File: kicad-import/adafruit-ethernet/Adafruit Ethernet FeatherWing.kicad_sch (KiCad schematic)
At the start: 48 parts

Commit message: Add initial annotation.
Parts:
- gave numbers to parts that had none: 48

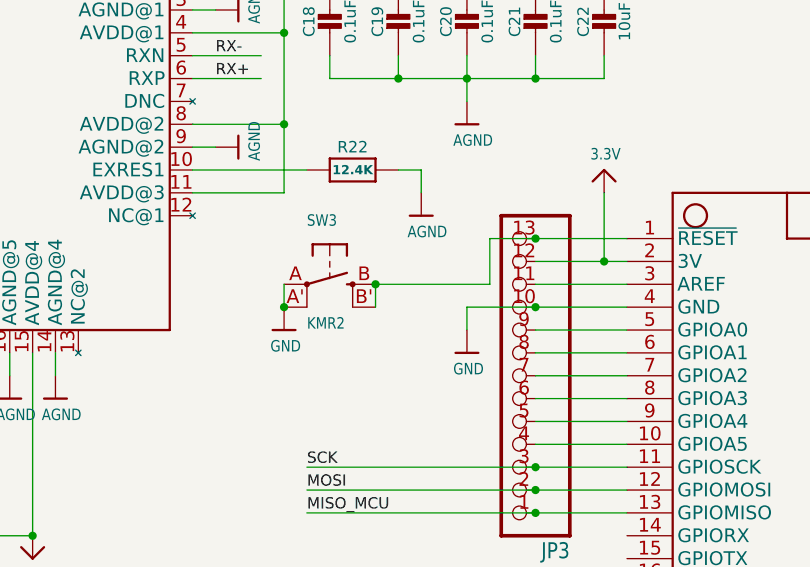
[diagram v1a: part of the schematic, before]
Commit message: Remove extra reset switches. Update notes.
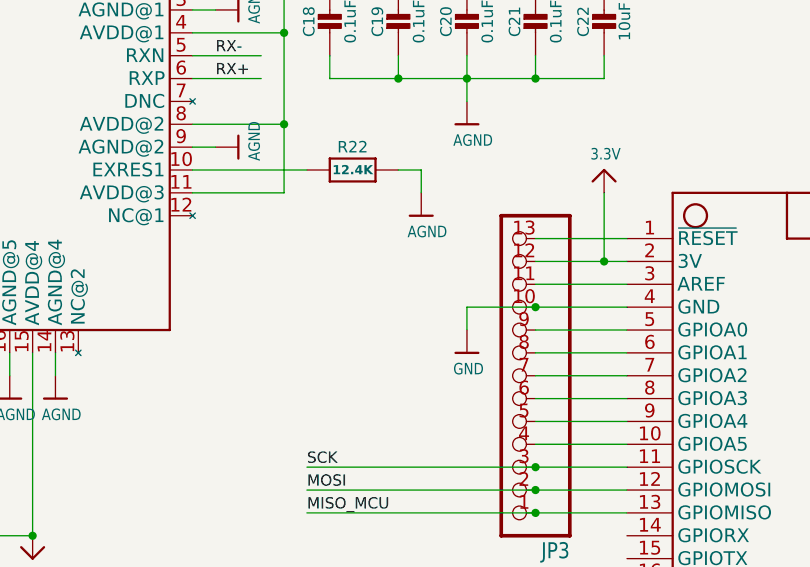
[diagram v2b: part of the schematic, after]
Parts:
- removed SW3: KMR2, Adafruit Ethernet FeatherWing:BTN_KMR2_4.6X2.8, symbol Adafruit Ethernet FeatherWing-eagle-import:SWITCH_TACT_SMT4.6X2.8
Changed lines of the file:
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@@
 	)
 	(junction
-		(at 154.94 106.68)
-		(diameter 0)
-		(color 0 0 0 0)
-	)
-	(junction
 		(at 154.94 88.9)
 		(diameter 0)
@@
 	)
 	(junction
-		(at 127 114.3)
-		(diameter 0)
-		(color 0 0 0 0)
-	)
-	(junction
 		(at 139.7 76.2)
 		(diameter 0)
@@
 	)
 	(junction
-		(at 137.16 111.76)
-		(diameter 0)
-		(color 0 0 0 0)
-	)
-	(junction
 		(at 213.36 132.08)
 		(diameter 0)
@@
 	(wire
 		(pts
-			(xy 137.16 111.76) (xy 137.16 114.3)
-		)
-		(stroke
-			(width 0.1524)
-			(type solid)
-		)
-	)
-	(wire
-		(pts
 			(xy 213.36 121.92) (xy 208.28 121.92)
 		)
@@
 	(wire
 		(pts
-			(xy 149.86 111.76) (xy 149.86 106.68)
-		)
-		(stroke
-			(width 0.1524)
-			(type solid)
-		)
-	)
-	(wire
-		(pts
 			(xy 40.64 99.06) (xy 40.64 101.6)
 		)
@@
 	(wire
 		(pts
-			(xy 127 111.76) (xy 127 114.3)
-		)
-		(stroke
-			(width 0.1524)
-			(type solid)
-		)
-	)
-	(wire
-		(pts
 			(xy 154.94 86.36) (xy 154.94 88.9)
 		)
@@
 	(wire
 		(pts
-			(xy 137.16 111.76) (xy 149.86 111.76)
-		)
-		(stroke
-			(width 0.1524)
-			(type solid)
-		)
-	)
-	(wire
-		(pts
 			(xy 76.2 58.42) (xy 76.2 55.88)
 		)
@@
 	(wire
 		(pts
-			(xy 149.86 106.68) (xy 154.94 106.68)
-		)
-		(stroke
-			(width 0.1524)
-			(type solid)
-		)
-	)
-	(wire
-		(pts
 			(xy 165.1 109.22) (xy 162.56 109.22)
 		)
@@
 	)
 	(symbol
-		(lib_id "Adafruit Ethernet FeatherWing-eagle-import:GND")
-		(at 127 116.84 0)
-		(unit 1)
-		(exclude_from_sim no)
-		(in_bom yes)
-		(on_board yes)
-		(dnp no)
-		(property "Reference" "#U$069"
-			(at 127 116.84 0)
-			(effects
-				(font
-					(size 1.27 1.27)
-				)
-				(hide yes)
-			)
-		)
-		(property "Value" "GND"
-			(at 125.476 119.38 0)
-			(effects
-				(font
-					(size 1.27 1.0795)
-				)
-				(justify left bottom)
-			)
-		)
-		(property "Footprint" ""
-			(at 127 116.84 0)
-			(effects
-				(font
-					(size 1.27 1.27)
-				)
-				(hide yes)
-			)
-		)
-		(property "Datasheet" ""
-			(at 127 116.84 0)
-			(effects
-				(font
-					(size 1.27 1.27)
-				)
-				(hide yes)
-			)
-		)
-		(property "Description" ""
-			(at 127 116.84 0)
-			(effects
-				(font
-					(size 1.27 1.27)
-				)
-				(hide yes)
-			)
-		)
-		(pin "1"
-		)
-		(instances
-			(project "Genesis"
-				(path "/66b8af00-4ede-44e3-a762-88857219665d/34668455-eab9-44a0-a7b2-48f3dfe2249d"
-					(reference "#U$069")
-					(unit 1)
-				)
-			)
-			(project ""
-				(path "/f8d80f0f-4921-491b-a5b2-8dada69d1b2b"
-					(reference "#U$47")
-					(unit 1)
-				)
-			)
-		)
-	)
-	(symbol
 		(lib_id "Adafruit Ethernet FeatherWing-eagle-import:AGND")
 		(at 88.9 154.94 0)
@@
 					(unit 1)
 				)
-			)
-		)
-	)
-	(symbol
-		(lib_id "Adafruit Ethernet FeatherWing-eagle-import:SWITCH_TACT_SMT4.6X2.8")
-		(at 132.08 111.76 0)
-		(unit 1)
-		(exclude_from_sim no)
-		(in_bom yes)
-		(on_board yes)
-		(dnp no)
-		(property "Reference" "SW3"
-			(at 129.54 105.41 0)
-			(effects
-				(font
-					(size 1.27 1.0795)
-				)
-				(justify left bottom)
-			)
-		)
-		(property "Value" "KMR2"
-			(at 129.54 116.84 0)
-			(effects
-				(font
-					(size 1.27 1.0795)
-				)
-				(justify left bottom)
-			)
-		)
-		(property "Footprint" "Adafruit Ethernet FeatherWing:BTN_KMR2_4.6X2.8"
-			(at 132.08 111.76 0)
-			(effects
-				(font
-					(size 1.27 1.27)
-				)
-				(hide yes)
-			)
-		)
-		(property "Datasheet" ""
-			(at 132.08 111.76 0)
-			(effects
-				(font
-					(size 1.27 1.27)
-				)
-				(hide yes)
-			)
-		)
-		(property "Description" ""
-			(at 132.08 111.76 0)
-			(effects
-				(font
-					(size 1.27 1.27)
-				)
-				(hide yes)
-			)
-		)
-		(pin "A"
-		)
-		(pin "A'"
-		)
-		(pin "B"
-		)
-		(pin "B'"
-		)
-		(instances
-			(project "Genesis"
-				(path "/66b8af00-4ede-44e3-a762-88857219665d/34668455-eab9-44a0-a7b2-48f3dfe2249d"
-					(reference "SW3")
-					(unit 1)
-				)
-			)
-			(project ""
-				(path "/f8d80f0f-4921-491b-a5b2-8dada69d1b2b"
-					(reference "SW1")
-					(unit 1)
-				)

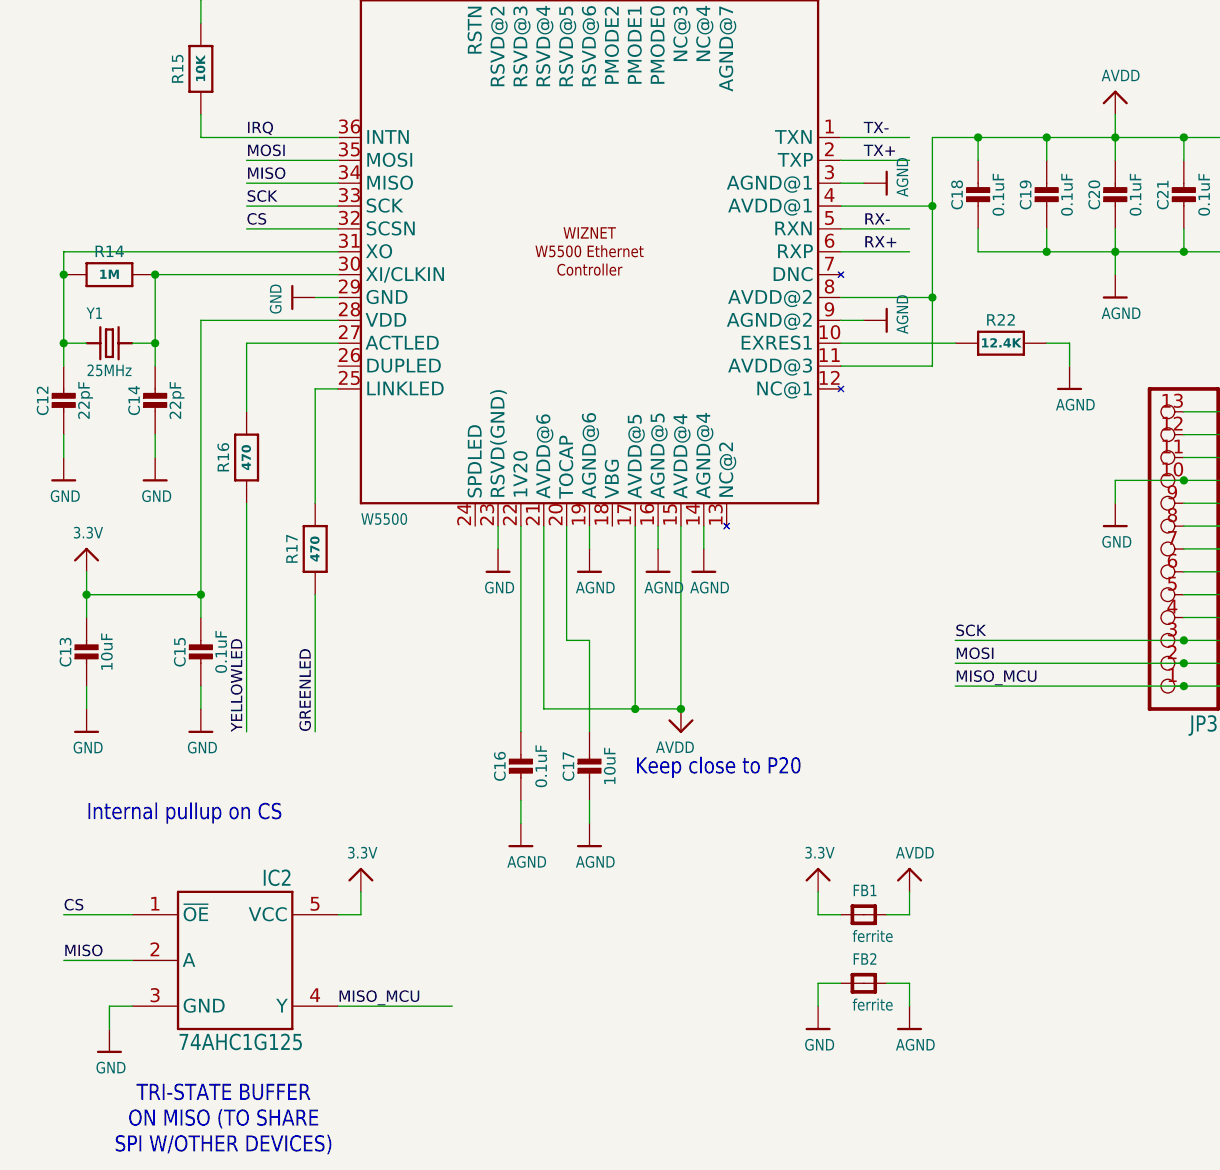
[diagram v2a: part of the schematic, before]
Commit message: Change power net on RTC page to match global. Change buffered MISO net name on ETH PHY to allow global MISO.
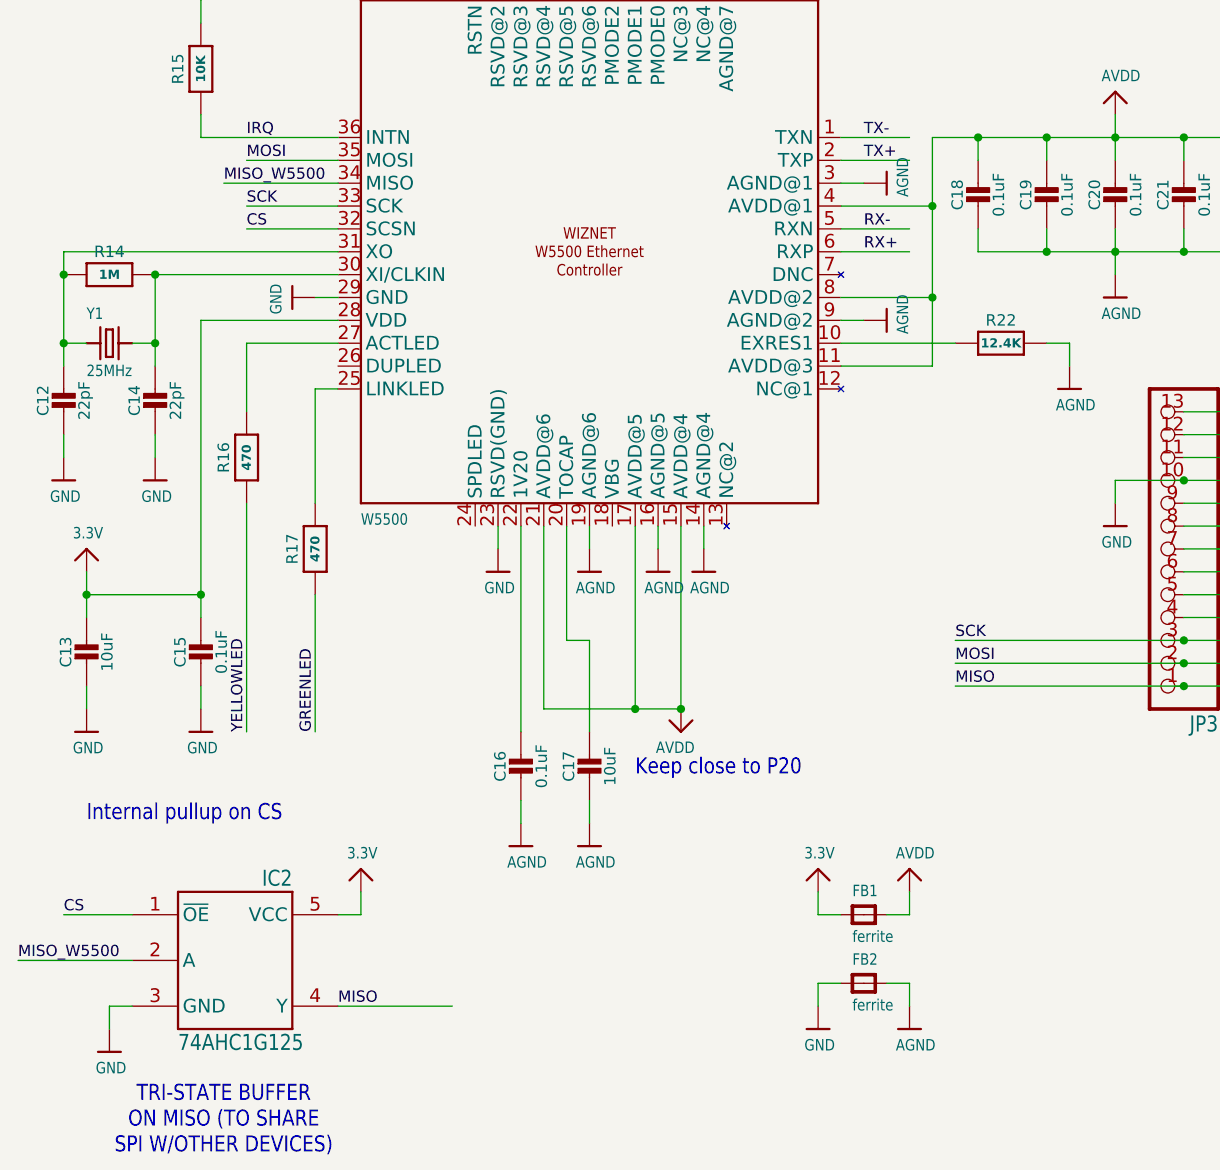
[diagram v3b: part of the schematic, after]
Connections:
- net MISO_MCU is gone; now on net MISO: IC2.4 (Y), JP3.1, MS1.13 (GPIOMISO)
- net MISO: no longer IC2.2 (A), U$5.34 (MISO)
- new net MISO_W5500: IC2.2 (A), U$5.34 (MISO)
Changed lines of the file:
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@@
 	(wire
 		(pts
-			(xy 60.96 81.28) (xy 50.8 81.28)
+			(xy 60.96 81.28) (xy 48.26 81.28)
 		)
 		(stroke
@@
 	(wire
 		(pts
-			(xy 30.48 167.64) (xy 38.1 167.64)
+			(xy 25.4 167.64) (xy 38.1 167.64)
 		)
 		(stroke
@@
 		)
 	)
-	(label "MISO_MCU"
+	(label "MISO"
 		(at 129.54 137.16 0)
 		(effects
@@
 		)
 	)
-	(label "MISO_MCU"
+	(label "MISO"
 		(at 60.96 172.72 0)
 		(effects
@@
 		)
 	)
-	(label "MISO"
-		(at 50.8 81.28 0)
+	(label "MISO_W5500"
+		(at 48.26 81.28 0)
 		(effects
 			(font
@@
 		)
 	)
-	(label "MISO"
-		(at 30.48 167.64 0)
-		(effects
-			(font
+	(label "MISO_W5500"
+		(at 25.4 167.64 0)
+		(effects
+			(font

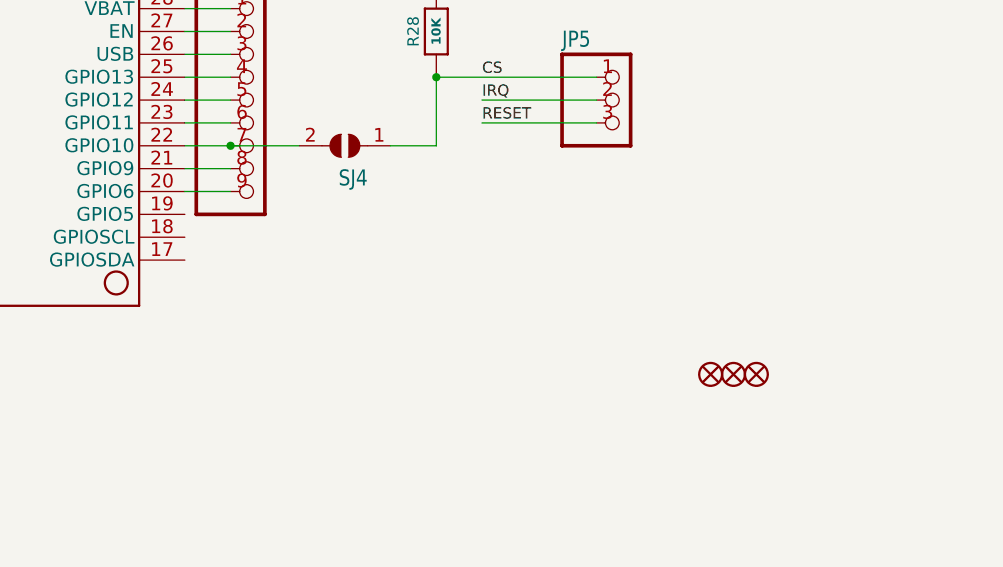
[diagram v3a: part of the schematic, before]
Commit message: Start adding heirarchical labels. Add notes to check sub-feather jumpers.
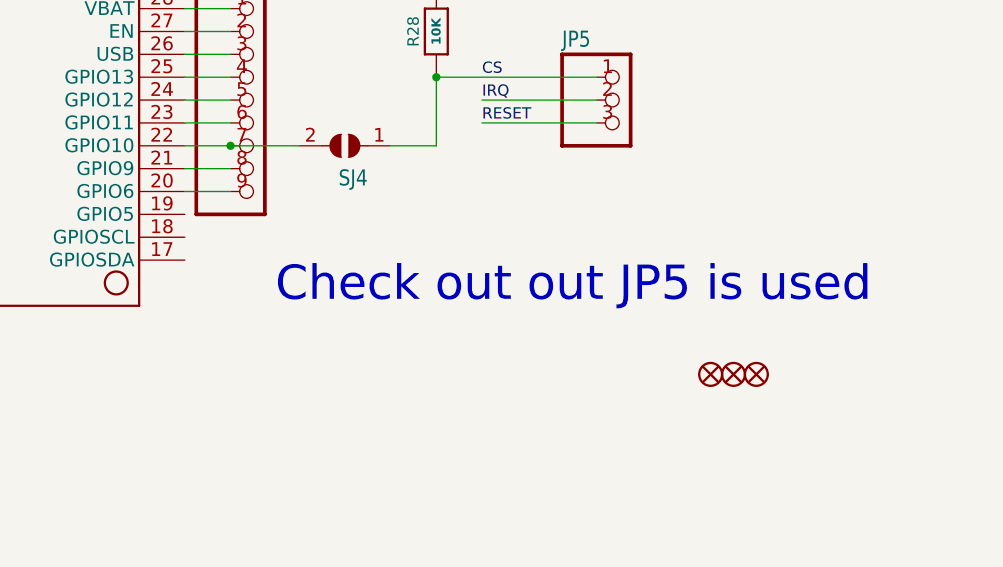
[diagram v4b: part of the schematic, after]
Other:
- note added: "Check out out JP5 is used"
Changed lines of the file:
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@@
+		)
+	)
+	(text "Check out out JP5 is used"
+		(exclude_from_sim no)
+		(at 251.46 147.574 0)
+		(effects
+			(font
+				(size 3.81 3.81)
+			)
 		)
 	)

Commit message: More updates.
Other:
- note added: "Check out how JP5 is used"
- note removed: "Check out out JP5 is used"
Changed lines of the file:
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@@
 		)
 	)
-	(text "Check out out JP5 is used"
+	(text "Check out how JP5 is used"
 		(exclude_from_sim no)
 		(at 251.46 147.574 0)

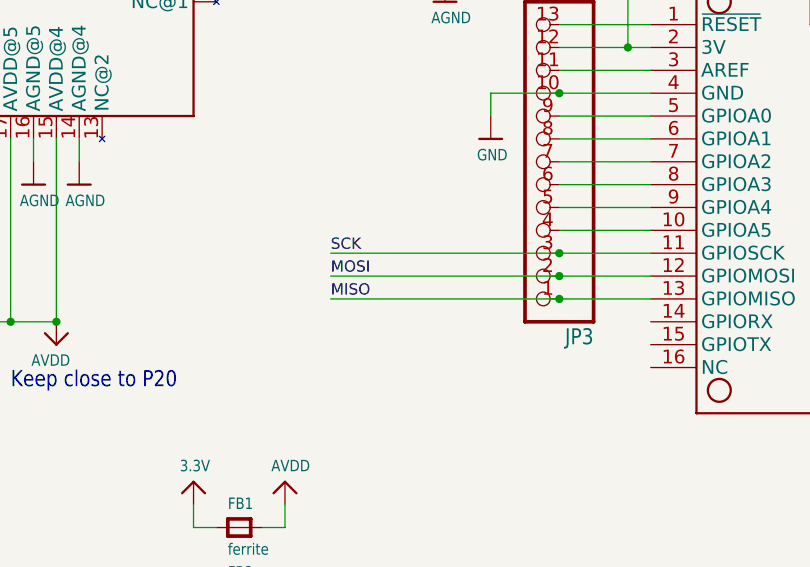
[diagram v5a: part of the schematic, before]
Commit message: Add and connect SPI sheet labels to Ethernet page.
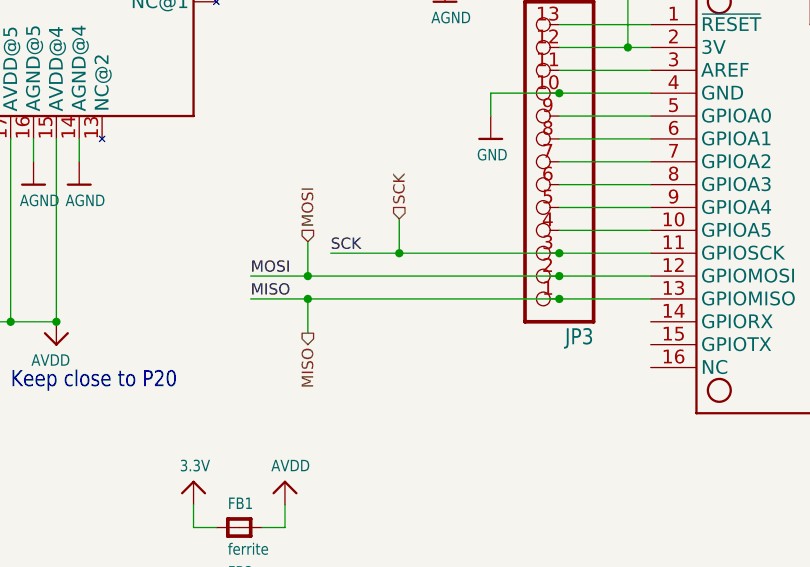
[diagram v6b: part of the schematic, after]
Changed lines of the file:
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@@
+	)
+	(junction
+		(at 127 137.16)
+		(diameter 0)
+		(color 0 0 0 0)
 	)
 	(junction
@@
 	)
 	(junction
+		(at 127 134.62)
+		(diameter 0)
+		(color 0 0 0 0)
+	)
+	(junction
 		(at 139.7 76.2)
 		(diameter 0)
@@
 	)
 	(junction
+		(at 137.16 132.08)
+		(diameter 0)
+		(color 0 0 0 0)
+	)
+	(junction
 		(at 139.7 88.9)
 		(diameter 0)
@@
 	(wire
 		(pts
+			(xy 127 137.16) (xy 154.94 137.16)
+		)
+		(stroke
+			(width 0.1524)
+			(type solid)
+		)
+	)
+	(wire
+		(pts
 			(xy 228.6 76.2) (xy 228.6 93.98)
 		)
@@
 	(wire
 		(pts
-			(xy 154.94 134.62) (xy 129.54 134.62)
+			(xy 154.94 134.62) (xy 127 134.62)
 		)
 		(stroke
@@
 	(wire
 		(pts
+			(xy 137.16 132.08) (xy 129.54 132.08)
+		)
+		(stroke
+			(width 0.1524)
+			(type solid)
+		)
+	)
+	(wire
+		(pts
 			(xy 220.98 132.08) (xy 213.36 132.08)
 		)
@@
 	(wire
 		(pts
-			(xy 129.54 137.16) (xy 154.94 137.16)
-		)
-		(stroke
-			(width 0.1524)
-			(type solid)
-		)
-	)
-	(wire
-		(pts
 			(xy 213.36 73.66) (xy 218.44 73.66)
 		)
@@
 	(wire
 		(pts
+			(xy 137.16 128.27) (xy 137.16 132.08)
+		)
+		(stroke
+			(width 0)
+			(type default)
+		)
+	)
+	(wire
+		(pts
 			(xy 109.22 30.48) (xy 109.22 33.02)
 		)
@@
 	(wire
 		(pts
+			(xy 120.65 137.16) (xy 127 137.16)
+		)
+		(stroke
+			(width 0.1524)
+			(type solid)
+		)
+	)
+	(wire
+		(pts
 			(xy 45.72 96.52) (xy 45.72 127)
 		)
@@
 	(wire
 		(pts
+			(xy 127 137.16) (xy 127 140.97)
+		)
+		(stroke
+			(width 0)
+			(type default)
+		)
+	)
+	(wire
+		(pts
 			(xy 154.94 88.9) (xy 162.56 88.9)
 		)
@@
 	(wire
 		(pts
-			(xy 154.94 132.08) (xy 129.54 132.08)
+			(xy 127 134.62) (xy 120.65 134.62)
+		)
+		(stroke
+			(width 0.1524)
+			(type solid)
+		)
+	)
+	(wire
+		(pts
+			(xy 154.94 132.08) (xy 137.16 132.08)
 		)
 		(stroke
@@
 			(width 0.1524)
 			(type solid)
+		)
+	)
+	(wire
+		(pts
+			(xy 127 130.81) (xy 127 134.62)
+		)
+		(stroke
+			(width 0)
+			(type default)
 		)
 	)
@@
 	)
 	(label "MISO"
-		(at 129.54 137.16 0)
+		(at 120.65 137.16 0)
 		(effects
 			(font
@@
 	)
 	(label "MOSI"
-		(at 129.54 134.62 0)
+		(at 120.65 134.62 0)
 		(effects
 			(font
@@
 		)
 	)
+	(hierarchical_label "MISO"
+		(shape output)
+		(at 127 140.97 270)
+		(effects
+			(font
+				(size 1.27 1.27)
+			)
+			(justify right)
+		)
+	)
+	(hierarchical_label "MOSI"
+		(shape input)
+		(at 127 130.81 90)
+		(effects
+			(font
+				(size 1.27 1.27)
+			)
+			(justify left)
+		)
+	)
+	(hierarchical_label "SCK"
+		(shape input)
+		(at 137.16 128.27 90)
+		(effects
+			(font
+				(size 1.27 1.27)
+			)
+			(justify left)
+		)
+	)
